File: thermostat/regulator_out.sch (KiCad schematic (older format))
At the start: 40 parts, among them J4 AVR-ISP-6, Q4 BC817, Q5 BSS806NL6327, Q6 BC817, Q7 BSS806NL6327, SW1 UP, SW2 DOWN, SW3 LEFT, SW4 RIGHT, SW5 OK, SW6 CANCEL, U6 ATmega328P-AU, U7 LM358, Y2 20MHz ABM3B

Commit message: Finished first PCB circuit draft. May not be optimal at all, regarding EMI etc.
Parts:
- added C32: 10n, Capacitor_SMD:C_0603_1608Metric, symbol Device:C
- RXD1: renamed from TP1; value TestPoint -> RXD
- TXD1: renamed from TP2; value TestPoint -> TXD
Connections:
- wire segments 157 -> 159
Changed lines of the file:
@@
 TXD
 $Comp
-L Connector:TestPoint TP1
+L Connector:TestPoint RXD1
 U 1 1 5F1A6BA3
 P 2900 3350
-F 0 "TP1" V 2854 3538 50  0000 L CNN
-F 1 "TestPoint" V 2945 3538 50  0000 L CNN
+F 0 "RXD1" V 2854 3538 50  0000 L CNN
+F 1 "RXD" V 2945 3538 50  0000 L CNN
 F 2 "TestPoint:TestPoint_Pad_D1.0mm" H 3100 3350 50  0001 C CNN
 F 3 "~" H 3100 3350 50  0001 C CNN
@@
 $EndComp
 $Comp
-L Connector:TestPoint TP2
+L Connector:TestPoint TXD1
 U 1 1 5F1A73A6
 P 2900 3450
-F 0 "TP2" V 2854 3638 50  0000 L CNN
-F 1 "TestPoint" V 2945 3638 50  0000 L CNN
+F 0 "TXD1" V 2854 3638 50  0000 L CNN
+F 1 "TXD" V 2945 3638 50  0000 L CNN
 F 2 "TestPoint:TestPoint_Pad_D1.0mm" H 3100 3450 50  0001 C CNN
 F 3 "~" H 3100 3450 50  0001 C CNN
@@
 NoConn ~ 1350 1950
 NoConn ~ 2550 2850
+$Comp
+L Device:C C32
+U 1 1 5E85A73E
+P 2900 6250
+F 0 "C32" H 3015 6296 50  0000 L CNN
+F 1 "10n" H 3015 6205 50  0000 L CNN
+F 2 "Capacitor_SMD:C_0603_1608Metric" H 2938 6100 50  0001 C CNN
+F 3 "~" H 2900 6250 50  0001 C CNN
+	1    2900 6250
+	1    0    0    -1
+$EndComp
+Wire Wire Line
+	2900 6050 2900 6100
+$Comp
+L power:GND #PWR?
+U 1 1 5E863ECC
+P 2900 6450
+AR Path="/5E863ECC" Ref="#PWR?"  Part="1"
+AR Path="/5E6A63AE/5E863ECC" Ref="#PWR04"  Part="1"
+F 0 "#PWR04" H 2900 6200 50  0001 C CNN
+F 1 "GND" H 2905 6277 50  0000 C CNN
+F 2 "" H 2900 6450 50  0001 C CNN
+F 3 "" H 2900 6450 50  0001 C CNN
+	1    2900 6450
+	1    0    0    -1
+$EndComp
+Wire Wire Line
+	2900 6450 2900 6400
 $EndSCHEMATC

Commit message: Deleted ATMega from schematics because I will only use the MKW41Z for everything.
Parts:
- removed C22, C23, C24: 100n, Capacitor_SMD:C_0603_1608Metric, symbol Device:C
- removed C25: 47n, Capacitor_SMD:C_0603_1608Metric, symbol Device:C
- removed C26, C27: 15p, Capacitor_SMD:C_0603_1608Metric, symbol Device:C
- removed J4: AVR-ISP-6, Connector_PinHeader_2.54mm:PinHeader_2x03_P2.54mm_Vertical_SMD, symbol Connector:AVR-ISP-6
- removed Q5, Q7: BSS806NL6327, Package_TO_SOT_SMD:SOT-23, symbol Device:Q_NMOS_GSD
- removed R12: 10K, Resistor_SMD:R_0603_1608Metric, symbol Device:R
- removed R16, R18: 4K7, Resistor_SMD:R_0603_1608Metric, symbol Device:R
- removed RXD1: RXD, TestPoint:TestPoint_Pad_D1.0mm, symbol Connector:TestPoint
- removed TXD1: TXD, TestPoint:TestPoint_Pad_D1.0mm, symbol Connector:TestPoint
- removed U6: ATmega328P-AU, Package_QFP:TQFP-32_7x7mm_P0.8mm, symbol MCU_Microchip_ATmega:ATmega328P-AU
- removed Y2: 20MHz ABM3B, Crystal:Crystal_SMD_Abracon_ABM3B-4Pin_5.0x3.2mm, symbol Device:Crystal_GND24
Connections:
- net labels removed: +3V3, INT_OUT, MISO, MOSI, RXD, SCK, SCL, SCL_A, SCL_B, SDA, SDA_A, SDA_B, TXD, avr_rst
- wire segments 159 -> 79
- no-connect marks 3 -> 0
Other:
- note removed: "ISP interface"
- note removed: "Voltage level shifter to allow the 5V AVR to \ncommunicate with the 3,3V ESP"

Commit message: Moved I2C peripherals into one schematic, moved GPIO peripherals onto main schematic.
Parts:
- removed D6: YELLOW, LED_SMD:LED_1210_3225Metric, symbol Device:LED
- removed D7: RED, LED_SMD:LED_1210_3225Metric, symbol Device:LED
- removed D8: GREEN, LED_SMD:LED_1210_3225Metric, symbol Device:LED
- removed R13, R14, R19: 1K8, Resistor_SMD:R_0603_1608Metric, symbol Device:R
- removed SW1: UP, Button_Switch_SMD:SW_SPST_Panasonic_EVQPL_3PL_5PL_PT_A08, symbol Switch:SW_Push
- removed SW2: DOWN, Button_Switch_SMD:SW_SPST_Panasonic_EVQPL_3PL_5PL_PT_A08, symbol Switch:SW_Push
- removed SW3: LEFT, Button_Switch_SMD:SW_SPST_Panasonic_EVQPL_3PL_5PL_PT_A08, symbol Switch:SW_Push
- removed SW4: RIGHT, Button_Switch_SMD:SW_SPST_Panasonic_EVQPL_3PL_5PL_PT_A08, symbol Switch:SW_Push
- removed SW5: OK, Button_Switch_SMD:SW_SPST_Panasonic_EVQPL_3PL_5PL_PT_A08, symbol Switch:SW_Push
- removed SW6: CANCEL, Button_Switch_SMD:SW_SPST_Panasonic_EVQPL_3PL_5PL_PT_A08, symbol Switch:SW_Push
- added C?: 22u, Capacitor_SMD:C_0805_2012Metric, symbol Device:C
- added C?: 100n, Capacitor_SMD:C_0603_1608Metric, symbol Device:C
- added C?: 2u2, Capacitor_SMD:C_0603_1608Metric, symbol Device:C
- added C?: 220u, Capacitor_SMD:CP_Elec_6.3x5.4, symbol Device:C
- added D?: SL03, Diode_SMD:D_SMF, symbol Device:D_Schottky
- added J?: Thermosthat, Connector_PinHeader_2.54mm:PinHeader_1x03_P2.54mm_Vertical_SMD_Pin1Left, symbol Connector_Generic:Conn_01x03
- added L?: 330u, Inductor_SMD:L_7.3x7.3_H3.5, symbol Device:L_Core_Iron
- added U?: LM2574M-5, Package_SO:SOIC-14W_7.5x9mm_P1.27mm, symbol Regulator_Switching:LM2574M-5
- added U?: LD1117S33TR_SOT223, Package_TO_SOT_SMD:SOT-223-3_TabPin2, symbol Regulator_Linear:LD1117S33TR_SOT223
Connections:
- net GNDA is gone; now on net GND: C28.2, C29.2, Q6.2 (E), R11.2, U7.4 (V-)
- net +36V: now also C?.1, J?.2 (Pin_2), U?.10 (VIN)
- net +5V: now also C?.1, C?.1, L?.2, U?.3 (FB), U?.3 (VI)
- net GND: now also C?.2, C?.2, C?.2, C?.2, D?.2 (A), J?.3 (Pin_3), U?.1 (GND), U?.4 (SGND), U?.5 (~ON~/OFF), U?.6 (PGND)
- net pwm_out: now also J?.1 (Pin_1)
- net ADC renamed SUPPLY_V
- net pwm_sig renamed REGULATOR_OUT
- new net: D?.1 (K), L?.1, U?.12 (OUT)
- new net +3V3: C?.1, U?.2 (VO)
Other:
- note added: "20V, 1A, E-LAB"
- note added: "3,3V is generated with an LDO fixed voltage supply"
- note added: "7-8-9 Port for Thermosthat control"
- note added: "Step-Down converter to transform variable ~~30V supply to 5V"
- note removed: "1,8V, 2mA"
- note removed: "Button matrix for basic input\nif WIFI is not available"
- note removed: "Signal LED with PWM option"
- moved on the sheet: C28, U7C

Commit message: Fixed orphaned symbols after Kicad library update. Kinetis MCU is now in upstream, thanks to me :)
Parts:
- L?: symbol Device:L_Core_Iron -> Device:L_Iron
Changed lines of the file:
@@
 	1    0    0    -1
-$EndComp
-Wire Wire Line
-	7300 2150 7300 2400
-$Comp
-L Device:R R15
-U 1 1 5E6AA7AC
-P 6800 1950
-F 0 "R15" V 6593 1950 50  0000 C CNN
-F 1 "4K7" V 6684 1950 50  0000 C CNN
-F 2 "Resistor_SMD:R_0603_1608Metric" V 6730 1950 50  0001 C CNN
-F 3 "~" H 6800 1950 50  0001 C CNN
-	1    6800 1950
-	0    1    1    0
 $EndComp
 $Comp
@@
 	1    0    0    -1
 $EndComp
-Wire Wire Line
-	6950 1950 7000 1950
 $Comp
 L power:+5V #PWR0157
@@
 Wire Wire Line
 	7300 1300 7300 1350
-Wire Wire Line
-	6600 1950 6650 1950
 $Comp
 L Amplifier_Operational:LM358 U7
@@
 $EndComp
 $Comp
-L Device:L_Core_Iron L?
+L Device:L_Iron L?
 U 1 1 5F453D97
 P -1600 1150
@@
 	2950 6050 2900 6050
 Connection ~ 2900 6050
+Wire Wire Line
+	7300 2150 7300 2400
+Wire Wire Line
+	6950 1950 7000 1950
+$Comp
+L Device:R R15
+U 1 1 5E6AA7AC
+P 6800 1950
+F 0 "R15" V 6593 1950 50  0000 C CNN
+F 1 "4K7" V 6684 1950 50  0000 C CNN
+F 2 "Resistor_SMD:R_0603_1608Metric" V 6730 1950 50  0001 C CNN
+F 3 "~" H 6800 1950 50  0001 C CNN
+	1    6800 1950
+	0    1    1    0
+$EndComp
+Wire Wire Line
+	6600 1950 6650 1950
 Text HLabel 6600 1950 0    50   Input ~ 0
 REGULATOR_OUT

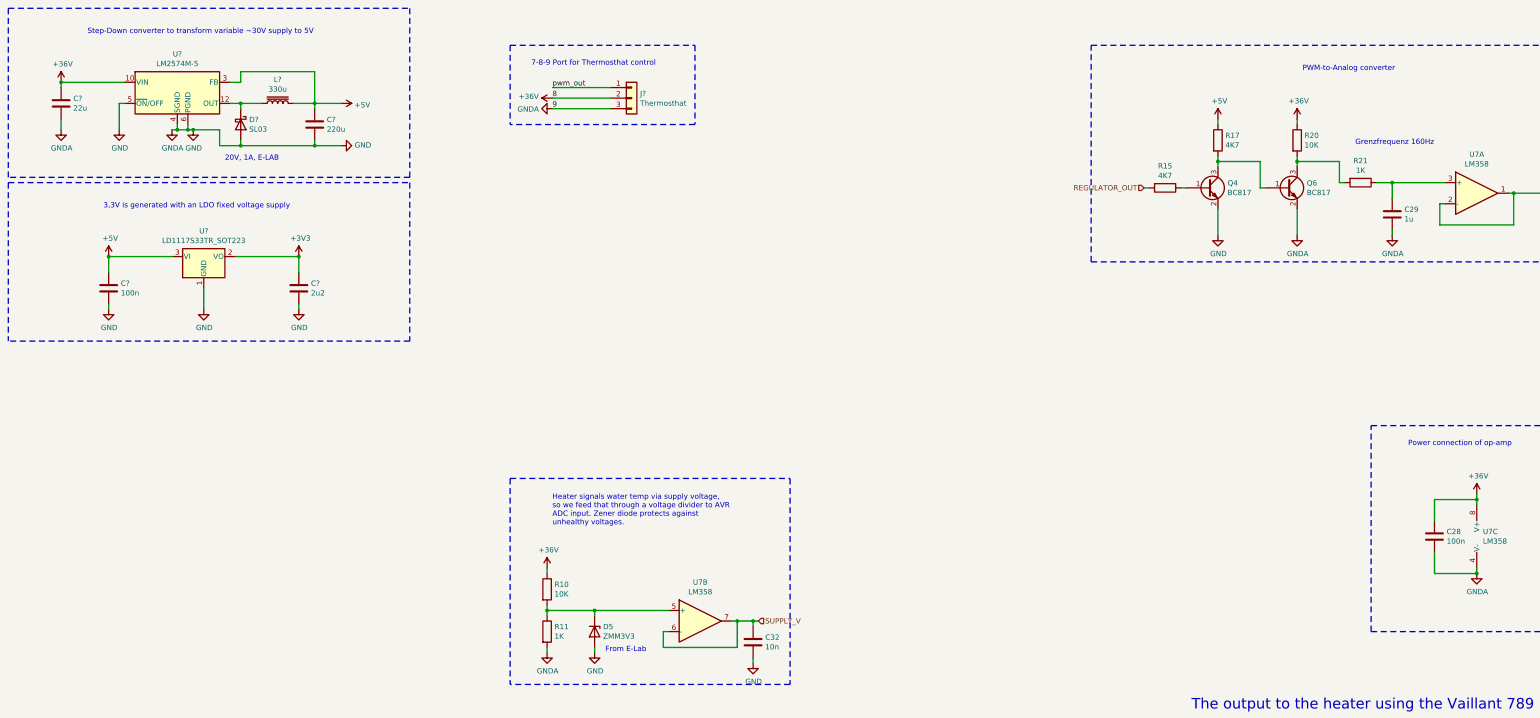
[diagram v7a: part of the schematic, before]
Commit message: Updated symbols after library update, some footprints still need to be assigned. Deleted PCB except for Display and buttons. Button arrangement wrong. Move buttons to other side of Display. Maybe put buttons on separate PCB and create one PCB for MCU and logic, since that needs to be a four layer one. That is expensive and should be kept as small as possible.
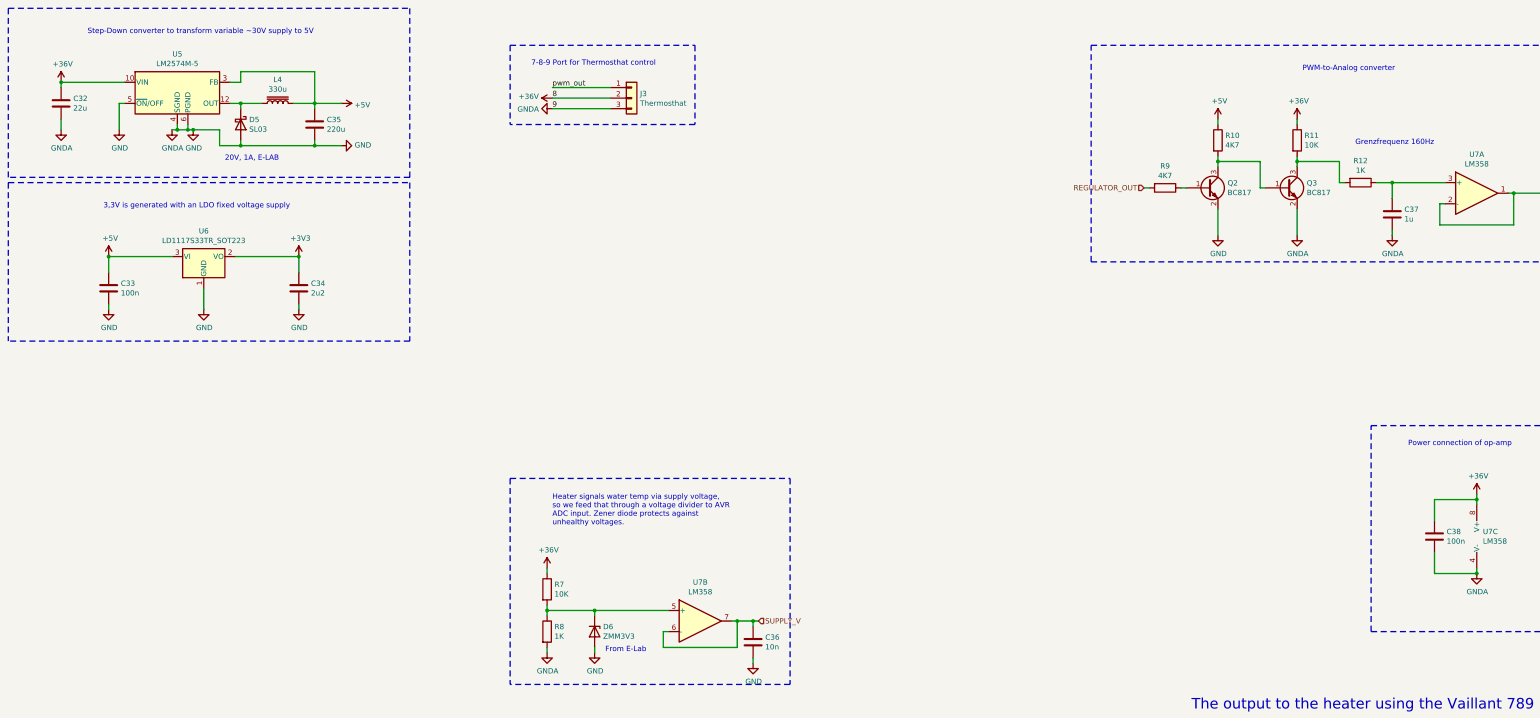
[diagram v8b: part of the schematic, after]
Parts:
- gave numbers to parts that had none: 9
- renumbered C32 to C36, C29 to C37, C28 to C38, D5 to D6, Q4 to Q2, Q6 to Q3, R17 to R10, R20 to R11, R21 to R12, R10 to R7, R11 to R8, R15 to R9
